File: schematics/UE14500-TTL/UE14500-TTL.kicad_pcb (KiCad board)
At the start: 2 copper layers, 76.8 x 99.1 mm, 46 parts, among them J1 Edge 1, J2 Edge 2, J3 5VDC IN, SW1 Power On, SW2 Reset, U1 74LS08, U10 74LS74, U11 74LS00, U12 74LS86, U13 74LS00, U14 74LS151, U15 74LS02, U16 74LS74, U2 74LS08, U3 74LS00, U4 74LS374, U5 74LS138, U6 74LS138, U7 74LS74, U8 74LS02, U9 74LS02

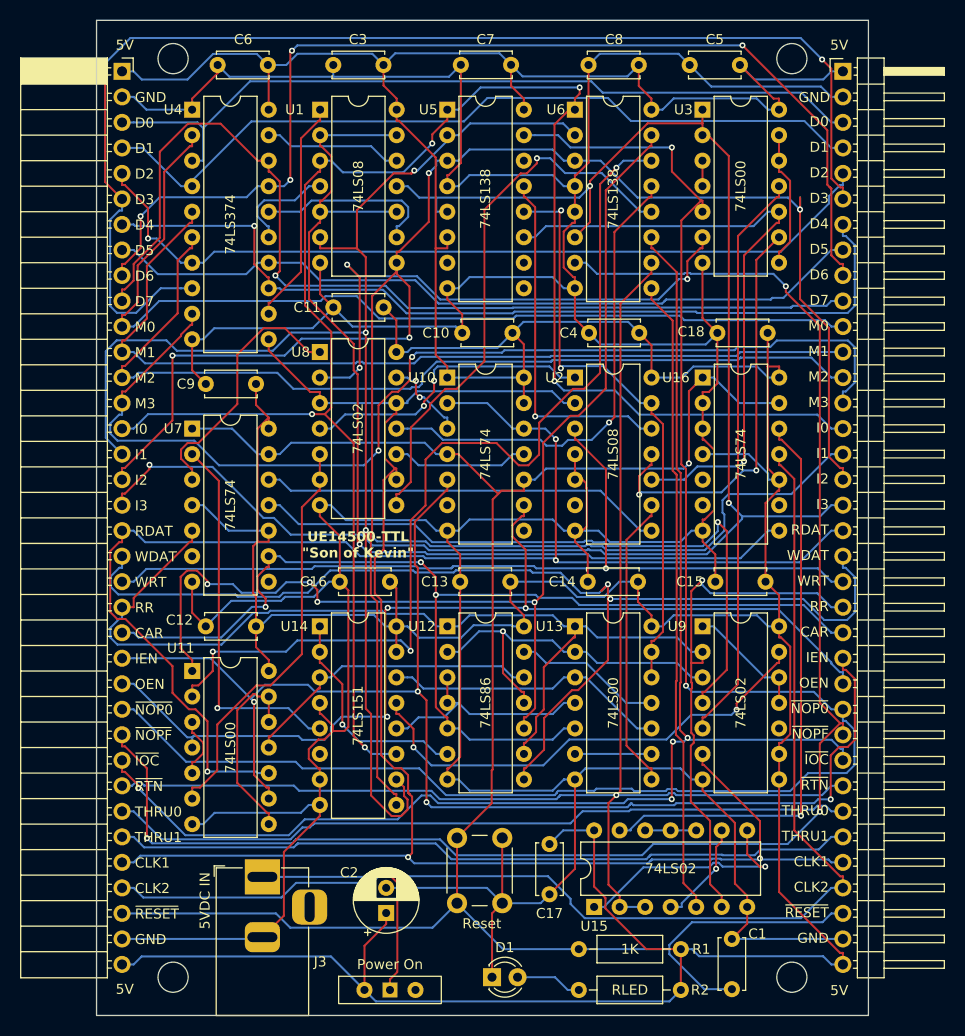
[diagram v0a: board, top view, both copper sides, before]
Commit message: Add a tape "REWIND" opcode to reset the PC early
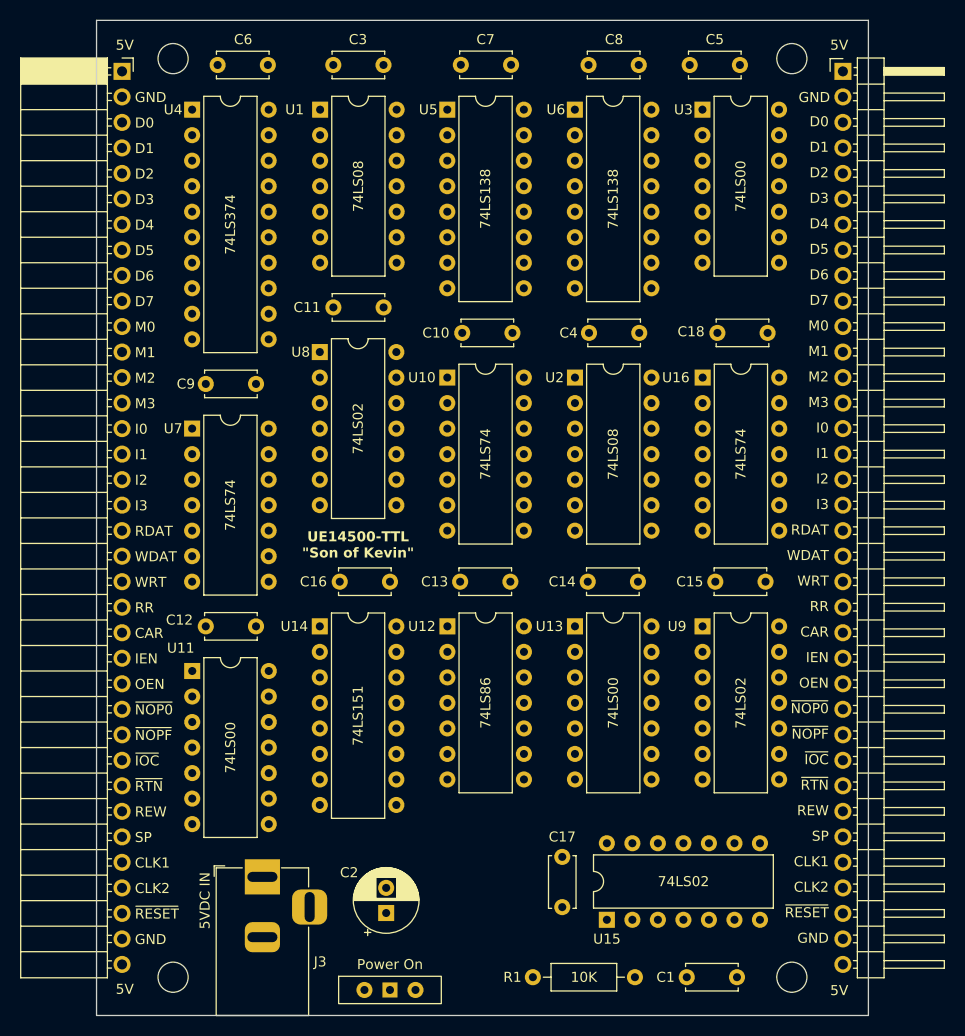
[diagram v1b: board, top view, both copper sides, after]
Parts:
- removed D1: Power, LED_THT:LED_D3.0mm
- removed R2: RLED, Resistor_THT:R_Axial_DIN0207_L6.3mm_D2.5mm_P10.16mm_Horizontal
- removed SW2: Reset, Button_Switch_THT:SW_PUSH_6mm
- R1: value 1K -> 10K
- moved R1 5.36 mm to (131.1, 143.5)
- moved C17 1.80 mm to (134.0, 131.5)
- moved U15 1.80 mm to (138.4, 137.8)
- moved C1 1.29 mm to (151.4, 143.5), turned to 180 degrees
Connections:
- net THRU1 renamed SPARE
- J1 pad 30: THRU0 -> OP_REWIND
- J2 pad 30: THRU0 -> OP_REWIND
- U2 pad 4: GND -> Net-(U2-Pad4)
- U2 pad 5: GND -> INST3
- U2 pad 6: unconnected-(U2-Pad6) -> OP_REWIND
- U9 pad 10: unconnected-(U9-Pad10) -> Net-(U2-Pad4)
- U9 pad 8: +5V -> ~{OP_NOP0}
- U9 pad 9: +5V -> ~{OP_NOP0}
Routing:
- net GND: track 513.9 -> 0.00 mm
- net +5V: track 508.3 -> 0.00 mm
- net ~{RESET}: track 200.3 -> 0.00 mm, vias 1 -> 0
- net INST1: track 192.6 -> 0.00 mm, vias 3 -> 0
- net INST2: track 186.9 -> 0.00 mm, vias 4 -> 0
- net INST0: track 178.8 -> 0.00 mm, vias 5 -> 0
- net ~{OP_NOP0}: track 173.2 -> 0.00 mm, vias 2 -> 0
- net CLK1: track 172.0 -> 0.00 mm, vias 2 -> 0
- net INST3: track 165.5 -> 0.00 mm, vias 3 -> 0
- net ~{OP_NOPF}: track 160.4 -> 0.00 mm, vias 3 -> 0
- net RR: track 145.3 -> 0.00 mm, vias 1 -> 0
- net ~{OP_RTN}: track 142.5 -> 0.00 mm, vias 1 -> 0
- net ~{OP_IOC}: track 136.7 -> 0.00 mm, vias 4 -> 0
- net RD_DATA: track 134.4 -> 0.00 mm, vias 3 -> 0
- net IEN: track 134.2 -> 0.00 mm, vias 4 -> 0
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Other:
- board text added: "REW"
- board text added: "SP"
- board text removed: "THRU0"
- board text removed: "THRU1"

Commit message: Make some renderings of the computer
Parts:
- renumbered C2 to C1, C1 to C2
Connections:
- net OP_REWIND renamed REWIND
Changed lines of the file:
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@@
 	(net 2 "+5V")
 	(net 3 "~{RESET}")
-	(net 4 "OP_REWIND")
+	(net 4 "REWIND")
 	(net 5 "CLK2")
 	(net 6 "OEN")
@@
 			)
 			(remove_unused_layers no)
-			(net 4 "OP_REWIND")
+			(net 4 "REWIND")
 			(pinfunction "Pin_30")
 			(pintype "passive")
@@
 		(descr "C, Disc series, Radial, pin pitch=5.00mm, , diameter*width=5*2.5mm^2, Capacitor, http://cdn-reichelt.de/documents/datenblatt/B300/DS_KERKO_TC.pdf")
 		(tags "C Disc series Radial pin pitch 5.00mm  diameter 5mm width 2.5mm Capacitor")
-		(property "Reference" "C1"
+		(property "Reference" "C2"
 			(at 7.112 0 180)
 			(layer "F.SilkS")
@@
 		)
 		(property "Value" "100nF"
-			(at 2.5 2.5 360)
+			(at 2.5 2.5 0)
 			(layer "F.Fab")
 			(effects
@@
 		)
 		(fp_text user "${REFERENCE}"
-			(at 2.5 0 360)
+			(at 2.5 0 0)
 			(layer "F.Fab")
 			(effects
@@
 		(descr "CP, Radial series, Radial, pin pitch=2.50mm, , diameter=6.3mm, Electrolytic Capacitor")
 		(tags "CP Radial series Radial pin pitch 2.50mm  diameter 6.3mm Electrolytic Capacitor")
-		(property "Reference" "C2"
+		(property "Reference" "C1"
 			(at 4.024 -3.684 180)
 			(layer "F.SilkS")
@@
 			)
 			(remove_unused_layers no)
-			(net 4 "OP_REWIND")
+			(net 4 "REWIND")
 			(pintype "output")
 		)
@@
 			)
 			(remove_unused_layers no)
-			(net 4 "OP_REWIND")
+			(net 4 "REWIND")
 			(pinfunction "Pin_30")
 			(pintype "passive")

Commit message: Lay out CPU board
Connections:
- net CAR_VAL renamed CAR_ALU
- net RR_VAL renamed RR_ALU
- U16 pad 9: unconnected-(U16B-Q-Pad9) -> SKIP
- U2 pad 5: INST3 -> MEM3
- U9 pad 9: ~{OP_NOP0} -> SKIP
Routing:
- net +5V: track 0.00 -> 499.8 mm
- net GND: track 0.00 -> 499.7 mm
- net ~{RESET}: track 0.00 -> 244.4 mm, vias 0 -> 1
- net CLK1: track 0.00 -> 185.2 mm, vias 0 -> 4
- net INST0: track 0.00 -> 178.5 mm, vias 0 -> 3
- net INST1: track 0.00 -> 176.1 mm, vias 0 -> 1
- net ~{OP_NOP0}: track 0.00 -> 168.8 mm, vias 0 -> 3
- net INST2: track 0.00 -> 156.9 mm, vias 0 -> 1
- net ~{OP_RTN}: track 0.00 -> 155.2 mm, vias 0 -> 2
- net INST3: track 0.00 -> 145.5 mm, vias 0 -> 3
- net ~{OP_IOC}: track 0.00 -> 143.1 mm, vias 0 -> 4
- net RR: track 0.00 -> 140.9 mm, vias 0 -> 3
- net RD_DATA: track 0.00 -> 131.9 mm, vias 0 -> 4
- net IEN: track 0.00 -> 126.9 mm, vias 0 -> 1
- net REWIND: track 0.00 -> 125.5 mm, vias 0 -> 2
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
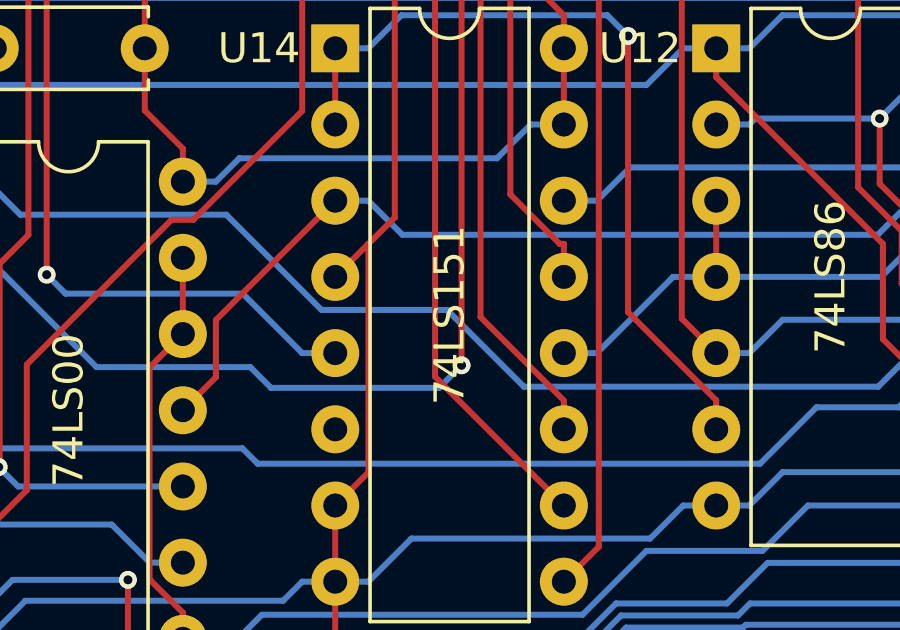
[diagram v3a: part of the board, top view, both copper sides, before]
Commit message: Change 74LS151 to 74LS251
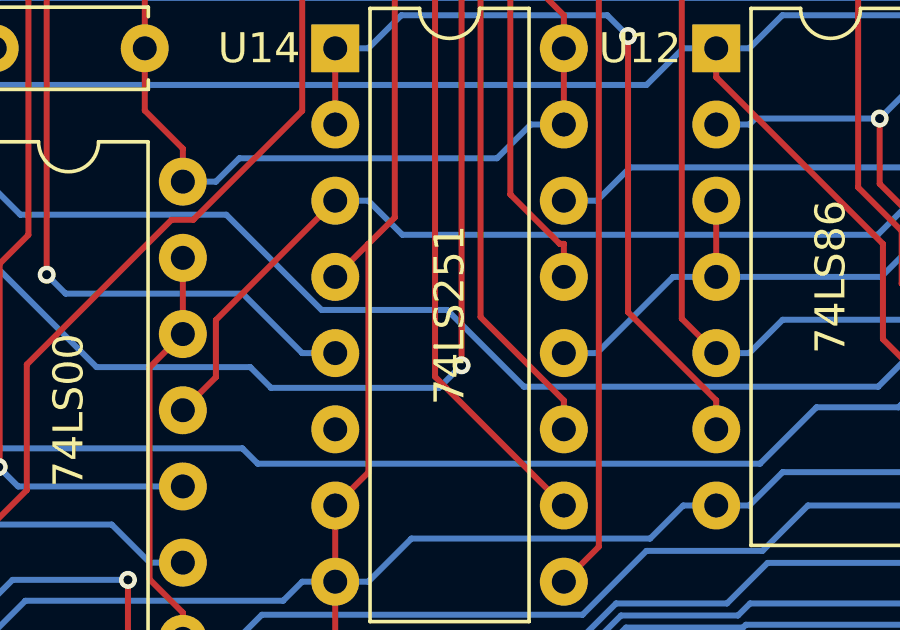
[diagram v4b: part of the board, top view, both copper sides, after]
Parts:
- U14: value 74LS151 -> 74LS251
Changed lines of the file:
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@@
 	(net 81 "Net-(U12-Pad13)")
 	(net 82 "Net-(U13-Pad6)")
-	(net 83 "unconnected-(U14-~{Z}-Pad6)")
+	(net 83 "unconnected-(U14-~{Y}-Pad6)")
 	(net 84 "Net-(U15-Pad4)")
 	(net 85 "Net-(U15-Pad10)")
@@
 			)
 		)
-		(property "Value" "74LS151"
+		(property "Value" "74LS251"
 			(at 3.81 8.89 90)
 			(layer "F.SilkS")
@@
 			)
 		)
-		(property "Datasheet" "http://www.ti.com/lit/gpn/sn74LS151"
+		(property "Datasheet" "http://www.ti.com/lit/gpn/sn74LS251"
 			(at 0 0 0)
 			(unlocked yes)
@@
 			)
 		)
-		(property "Description" "Multiplexer 8 to 1"
+		(property "Description" "Multiplexer 8 to 1, 3-state Outputs"
 			(at 0 0 0)
 			(unlocked yes)
@@
 			(remove_unused_layers no)
 			(net 92 "RR_ALU")
-			(pinfunction "Z")
-			(pintype "output")
+			(pinfunction "Y")
+			(pintype "tri_state")
 		)
 		(pad "6" thru_hole oval
@@
 			)
 			(remove_unused_layers no)
-			(net 83 "unconnected-(U14-~{Z}-Pad6)")
-			(pinfunction "~{Z}")
-			(pintype "output+no_connect")
+			(net 83 "unconnected-(U14-~{Y}-Pad6)")
+			(pinfunction "~{Y}")
+			(pintype "tri_state+no_connect")
 		)
 		(pad "7" thru_hole oval
@@
 			(remove_unused_layers no)
 			(net 1 "GND")
-			(pinfunction "~{E}")
-			(pintype "input")
-		)
+			(pinfunction "~{OE}")
+			(pintype "input")
+		)
